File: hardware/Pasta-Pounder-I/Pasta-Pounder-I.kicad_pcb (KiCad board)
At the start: 2 copper layers, 70 x 20 mm, 59 parts, among them CN1 XT30UPB-M, J1 USB_C_Receptacle, J10 Motor_2-, J11 ESC_VCC, J12 ESC_GND, J4 ESC_Port, J5 JST-SH, J7 Motor_1+, J8 Motor_1-, J9 Motor_2+, Q1 AO3401A, SW1 RESET-SW, SW2 BOOT-SW, SW3 5.8 ZSPT, U1 DRV8874PWPR, U2 DRV8874PWPR, U3 ESP32-S3-MINI-1U, U4 USBLC6-2P6, U7 SY8113BADC

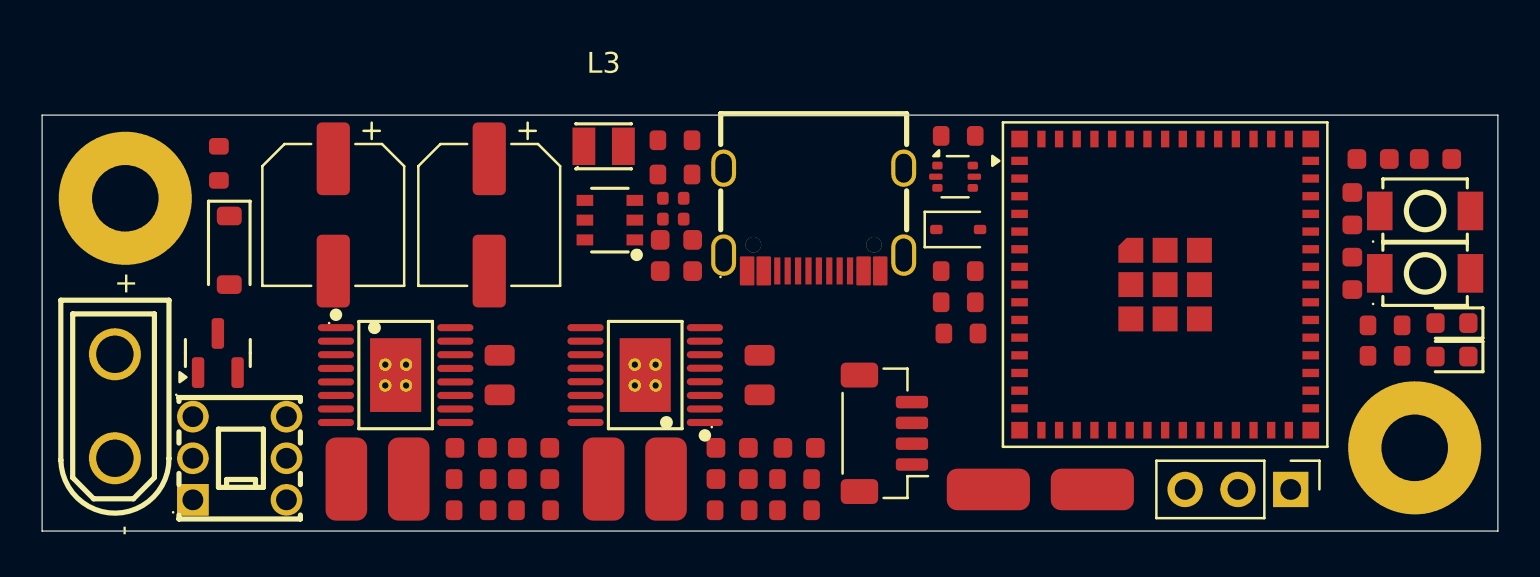
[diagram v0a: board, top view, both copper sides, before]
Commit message: Converted board from 2 -> 4 layer board
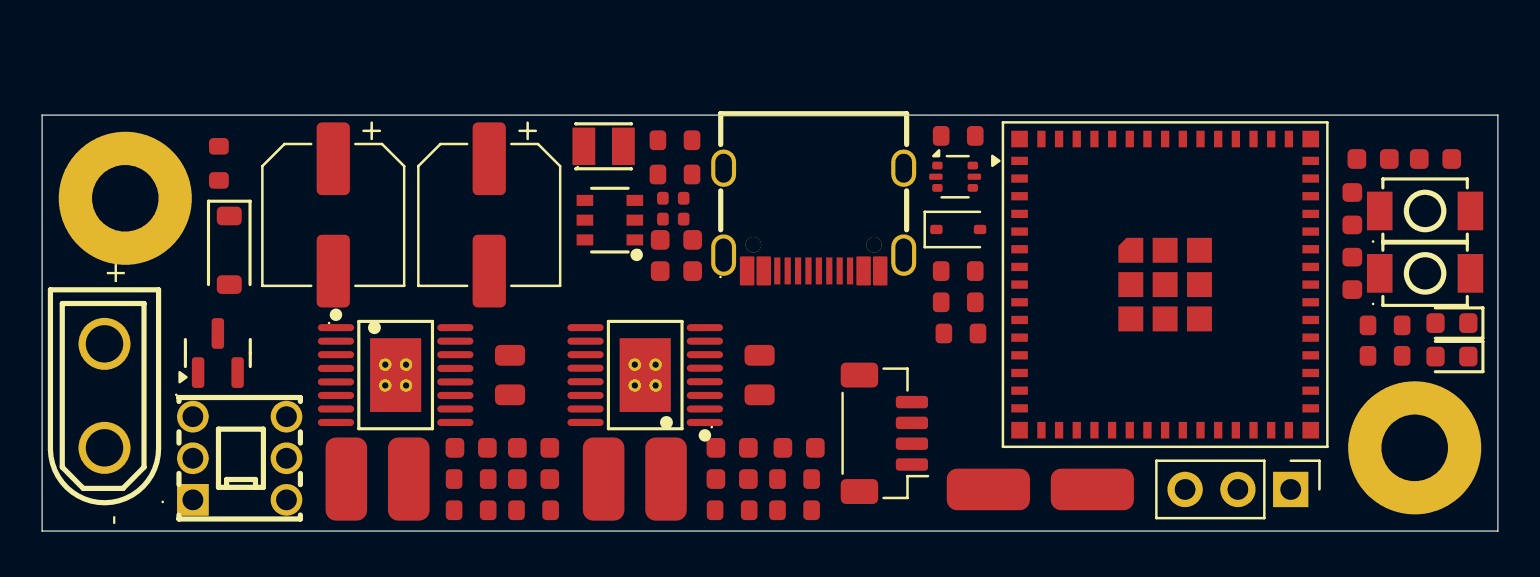
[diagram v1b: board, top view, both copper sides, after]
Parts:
- moved CN1 0.71 mm to (117.5, 103.0)
- moved C8 0.50 mm to (137.0, 102.0)
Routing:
- added copper zone on In1.Cu, net GND
- added copper zone on In2.Cu, net VCC
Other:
- copper layers 2 -> 4
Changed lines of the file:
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@@
 	(layers
 		(0 "F.Cu" signal)
+		(4 "In1.Cu" power)
+		(6 "In2.Cu" power)
 		(2 "B.Cu" signal)
 		(9 "F.Adhes" user "F.Adhesive")
@@
 	)
 	(setup
+		(stackup
+			(layer "F.SilkS"
+				(type "Top Silk Screen")
+			)
+			(layer "F.Paste"
+				(type "Top Solder Paste")
+			)
+			(layer "F.Mask"
+				(type "Top Solder Mask")
+				(thickness 0.01)
+			)
+			(layer "F.Cu"
+				(type "copper")
+				(thickness 0.035)
+			)
+			(layer "dielectric 1"
+				(type "prepreg")
+				(thickness 0.1)
+				(material "FR4")
+				(epsilon_r 4.5)
+				(loss_tangent 0.02)
+			)
+			(layer "In1.Cu"
+				(type "copper")
+				(thickness 0.035)
+			)
+			(layer "dielectric 2"
+				(type "core")
+				(thickness 1.24)
+				(material "FR4")
+				(epsilon_r 4.5)
+				(loss_tangent 0.02)
+			)
+			(layer "In2.Cu"
+				(type "copper")
+				(thickness 0.035)
+			)
+			(layer "dielectric 3"
+				(type "prepreg")
+				(thickness 0.1)
+				(material "FR4")
+				(epsilon_r 4.5)
+				(loss_tangent 0.02)
+			)
+			(layer "B.Cu"
+				(type "copper")
+				(thickness 0.035)
+			)
+			(layer "B.Mask"
+				(type "Bottom Solder Mask")
+				(thickness 0.01)
+			)
+			(layer "B.Paste"
+				(type "Bottom Solder Paste")
+			)
+			(layer "B.SilkS"
+				(type "Bottom Silk Screen")
+			)
+			(copper_finish "None")
+			(dielectric_constraints no)
+		)
 		(pad_to_mask_clearance 0)
 		(allow_soldermask_bridges_in_footprints no)
@@
 		(capping no)
 		(filling no)
+		(zone_defaults)
 		(pcbplotparams
 			(layerselection 0x00000000_00000000_55555555_5755f5ff)
@@
 	(footprint "lcsc_footprints:C428721_CONN-TH_XT30UPB-M"
 		(layer "F.Cu")
-		(at 118 103.5 90)
+		(at 117.5 103 90)
 		(property "Reference" "CN1"
 			(at 0 -4 90)
@@
 			(at 0 -4 0)
 			(layer "F.SilkS")
+			(hide yes)
 			(effects
 				(font
@@
 	(footprint "PCM_JLCPCB:C_0805"
 		(layer "F.Cu")
-		(at 136.5 102 -90)
+		(at 137 102 -90)
 		(descr "Capacitor SMD 0805 (2012 Metric), square (rectangular) end terminal, IPC_7351 nominal, (Body size source: IPC-SM-782 page 76, https://www.pcb-3d.com/wordpress/wp-content/uploads/ipc-sm-782a_amendment_1_and_2.pdf, https://docs.google.com/spreadsheets/d/1BsfQQcO9C6DZCsRaXUlFlo91Tg2WpOkGARC1WS5S8t0/edit?usp=sharing), generated with kicad-footprint-generator")
 		(tags "capacitor")
@@
 			(at 0 7.12 90)
 			(layer "F.Fab")
+			(hide yes)
 			(effects
 				(font
@@
 			)
 		)
+		(model "${KIPRJMOD}/libs/lcsc/3dmodels/C2980299.step"
+			(offset
+				(xyz 0 0 0)
+			)
+			(scale
+				(xyz 1 1 1)
+			)
+			(rotate
+				(xyz 0 0 0)
+			)
+		)
 	)
 	(footprint "PCM_JLCPCB:C_0603"
@@
 		(layer "Edge.Cuts")
 	)
+	(zone
+		(net "GND")
+		(layer "In1.Cu")
+		(hatch edge 0.5)
+		(connect_pads
+			(clearance 0.5)
+		)
+		(min_thickness 0.25)
+		(fill
+			(thermal_gap 0.5)
+			(thermal_bridge_width 0.5)
+			(island_removal_mode 0)
+		)
+		(polygon
+			(pts
+				(xy 114 89) (xy 185 89) (xy 185 110) (xy 114 110)
+			)
+		)
+	)
+	(zone
+		(net "VCC")
+		(layer "In2.Cu")
+		(hatch edge 0.5)
+		(priority 1)
+		(connect_pads
+			(clearance 0.5)
+		)
+		(min_thickness 0.25)
+		(fill
+			(thermal_gap 0.5)
+			(thermal_bridge_width 0.5)
+			(island_removal_mode 0)
+		)
+		(polygon
+			(pts
+				(xy 114 89) (xy 185 89) (xy 185 110) (xy 114 110)
+			)
+		)
+	)
 	(embedded_fonts no)

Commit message: Miscelaneous PCB changes
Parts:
- moved C6 3.13 mm to (135.0, 105.5)
- moved R5 3.13 mm to (135.0, 108.5)
- moved R6 2.87 mm to (138.0, 108.5)
- moved R7 2.87 mm to (138.0, 107.0)
- moved C5 1.51 mm to (135.0, 107.0)
- moved C7 1.51 mm to (138.0, 105.5)
- moved C11 0.12 mm to (150.8, 105.5)
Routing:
- added copper zone on In2.Cu, net +3V3
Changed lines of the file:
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@@
 		(capping no)
 		(filling no)
-		(zone_defaults)
 		(pcbplotparams
 			(layerselection 0x00000000_00000000_55555555_5755f5ff)
@@
 	(footprint "PCM_JLCPCB:R_0603"
 		(layer "F.Cu")
-		(at 135.13 108.5 180)
+		(at 138 108.5 180)
 		(descr "Resistor SMD 0603 (1608 Metric), square (rectangular) end terminal, IPC_7351 nominal, (Body size source: IPC-SM-782 page 72, https://www.pcb-3d.com/wordpress/wp-content/uploads/ipc-sm-782a_amendment_1_and_2.pdf), generated with kicad-footprint-generator")
 		(tags "resistor")
@@
 	(footprint "PCM_JLCPCB:R_0603"
 		(layer "F.Cu")
-		(at 138.13 108.5)
+		(at 135 108.5)
 		(descr "Resistor SMD 0603 (1608 Metric), square (rectangular) end terminal, IPC_7351 nominal, (Body size source: IPC-SM-782 page 72, https://www.pcb-3d.com/wordpress/wp-content/uploads/ipc-sm-782a_amendment_1_and_2.pdf), generated with kicad-footprint-generator")
 		(tags "resistor")
@@
 	(footprint "PCM_JLCPCB:C_0603"
 		(layer "F.Cu")
-		(at 138.13 107)
+		(at 138 105.5)
 		(descr "Capacitor SMD 0603 (1608 Metric), square (rectangular) end terminal, IPC_7351 nominal, (Body size source: IPC-SM-782 page 76, https://www.pcb-3d.com/wordpress/wp-content/uploads/ipc-sm-782a_amendment_1_and_2.pdf), generated with kicad-footprint-generator")
 		(tags "capacitor")
@@
 	(footprint "PCM_JLCPCB:C_0603"
 		(layer "F.Cu")
-		(at 150.9 105.5 180)
+		(at 150.78 105.5 180)
 		(descr "Capacitor SMD 0603 (1608 Metric), square (rectangular) end terminal, IPC_7351 nominal, (Body size source: IPC-SM-782 page 76, https://www.pcb-3d.com/wordpress/wp-content/uploads/ipc-sm-782a_amendment_1_and_2.pdf), generated with kicad-footprint-generator")
 		(tags "capacitor")
@@
 		)
 		(fp_text user "${REFERENCE}"
-			(at 0 0.37 0)
+			(at 0 0 0)
 			(layer "F.Fab")
 			(effects
@@
 	(footprint "PCM_JLCPCB:R_0603"
 		(layer "F.Cu")
-		(at 135.13 107 180)
+		(at 138 107 180)
 		(descr "Resistor SMD 0603 (1608 Metric), square (rectangular) end terminal, IPC_7351 nominal, (Body size source: IPC-SM-782 page 72, https://www.pcb-3d.com/wordpress/wp-content/uploads/ipc-sm-782a_amendment_1_and_2.pdf), generated with kicad-footprint-generator")
 		(tags "resistor")
@@
 	(footprint "PCM_JLCPCB:C_0603"
 		(layer "F.Cu")
-		(at 138.13 105.5)
+		(at 135 105.5)
 		(descr "Capacitor SMD 0603 (1608 Metric), square (rectangular) end terminal, IPC_7351 nominal, (Body size source: IPC-SM-782 page 76, https://www.pcb-3d.com/wordpress/wp-content/uploads/ipc-sm-782a_amendment_1_and_2.pdf), generated with kicad-footprint-generator")
 		(tags "capacitor")
@@
 	(footprint "PCM_JLCPCB:C_0603"
 		(layer "F.Cu")
-		(at 135.13 105.5)
+		(at 135 107)
 		(descr "Capacitor SMD 0603 (1608 Metric), square (rectangular) end terminal, IPC_7351 nominal, (Body size source: IPC-SM-782 page 76, https://www.pcb-3d.com/wordpress/wp-content/uploads/ipc-sm-782a_amendment_1_and_2.pdf), generated with kicad-footprint-generator")
 		(tags "capacitor")
@@
 		(polygon
 			(pts
-				(xy 114 89) (xy 185 89) (xy 185 110) (xy 114 110)
+				(xy 114 89) (xy 140.000889 89.002313) (xy 140 99) (xy 131.5 99) (xy 131.5 105) (xy 143.5 105) (xy 143.5 99)
+				(xy 155.5 99) (xy 155.5 110) (xy 114 110)
+			)
+		)
+	)
+	(zone
+		(net "+3V3")
+		(layer "In2.Cu")
+		(hatch edge 0.5)
+		(priority 2)
+		(connect_pads
+			(clearance 0.5)
+		)
+		(min_thickness 0.25)
+		(fill
+			(thermal_gap 0.5)
+			(thermal_bridge_width 0.5)
+			(island_removal_mode 0)
+		)
+		(polygon
+			(pts
+				(xy 185 89) (xy 140.000889 89.002313) (xy 140 99) (xy 131.5 99) (xy 131.5 105) (xy 143.5 105) (xy 143.5 99)
+				(xy 155.5 99) (xy 155.5 110) (xy 185 110)
 			)
 		)
